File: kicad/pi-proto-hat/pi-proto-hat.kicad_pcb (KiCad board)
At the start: 2 copper layers, 65 x 56 mm, 5 parts, among them P1 Conn_02x20_Odd_Even

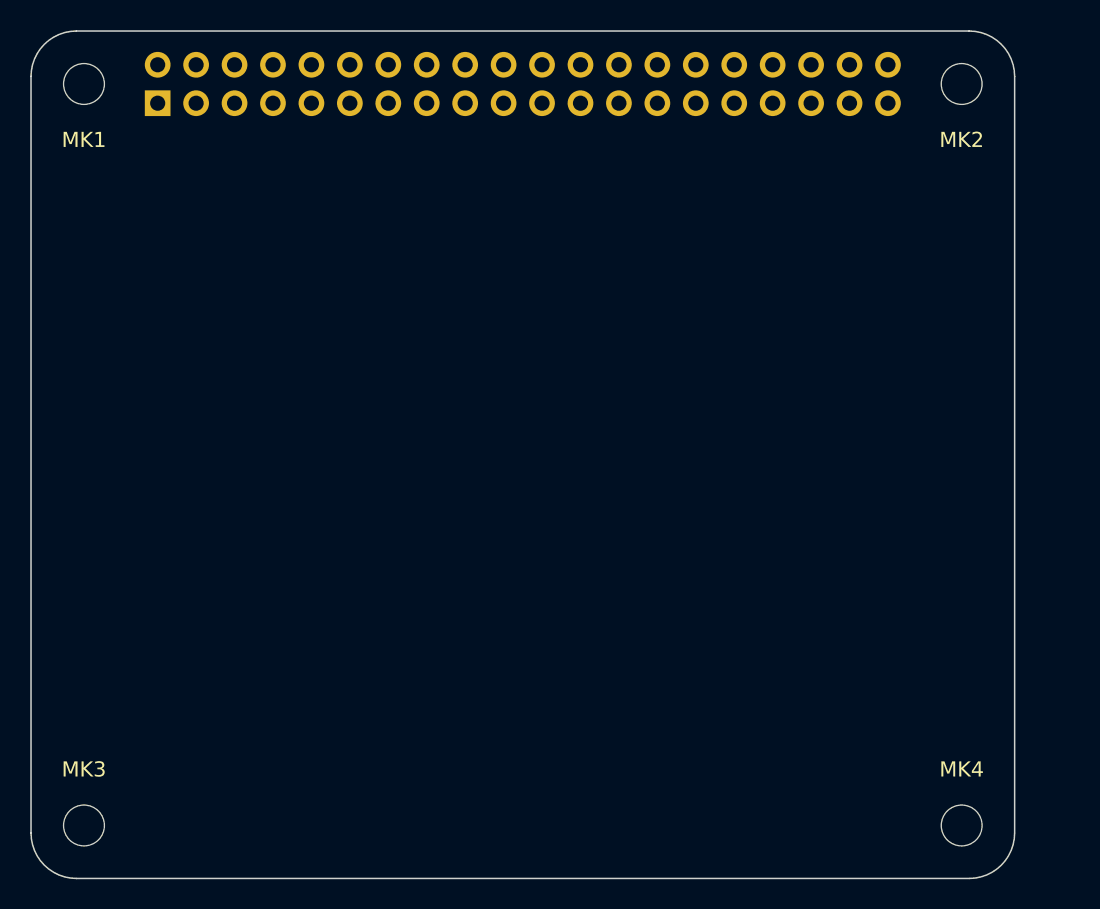
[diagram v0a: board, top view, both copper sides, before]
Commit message: R1: one GPIO connector, one I2C connector
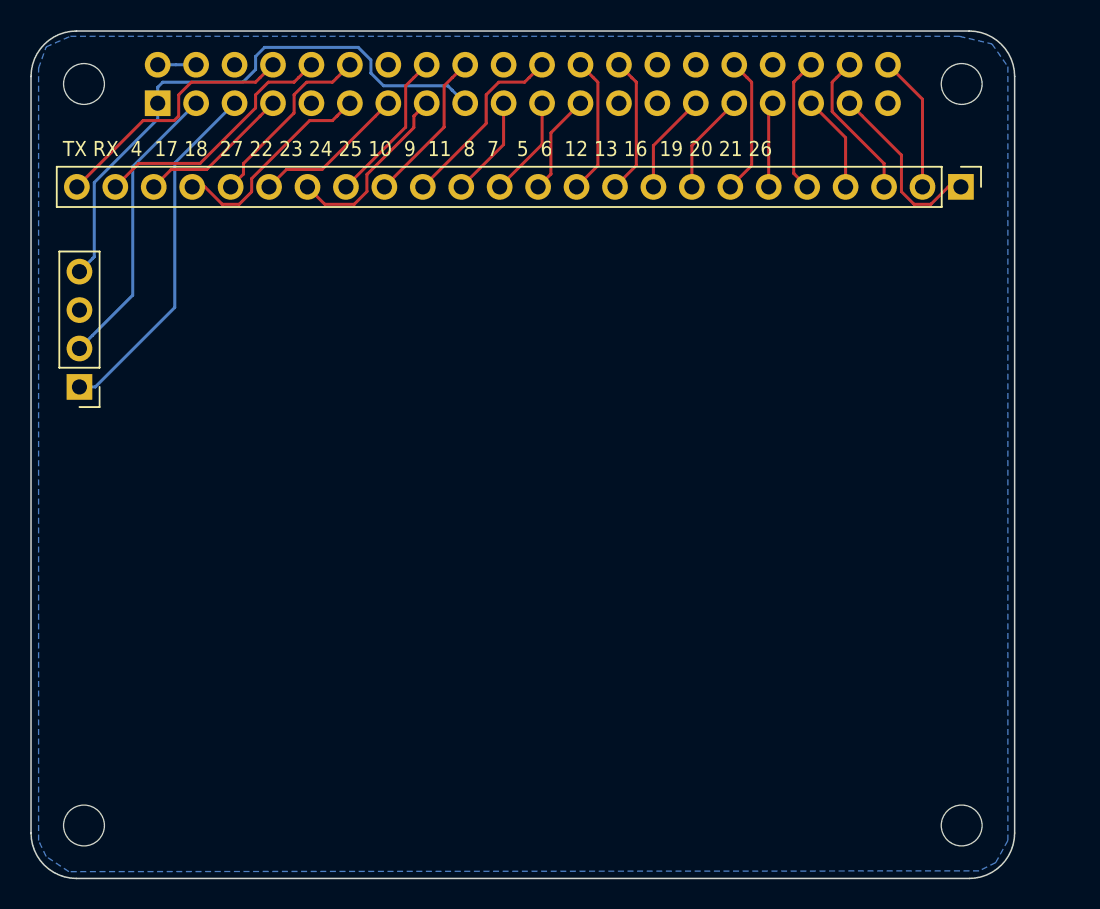
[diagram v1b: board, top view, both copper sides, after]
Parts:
- added J1: Conn_01x24_Male, Connector_PinHeader_2.54mm:PinHeader_1x24_P2.54mm_Vertical, F.Cu at (261.4, 104.3)
- added J2: Conn_I2C, Connector_PinHeader_2.54mm:PinHeader_1x04_P2.54mm_Vertical, F.Cu at (203.2, 117.5)
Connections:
- net /ID_SC renamed Net-(P1-Pad28)
- net /ID_SD renamed Net-(P1-Pad27)
- P1 pad 24: /GPIO8(SPI0_CE_N) -> /GPIO8(SPI0_CE_0)
- P1 pad 26: /GPIO7(SPI1_CE_N) -> /GPIO7(SPI1_CE_1)
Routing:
- net +3V3: track 0.00 -> 38.3 mm
- net /GPIO3(SCL1): track 0.00 -> 23.6 mm
- net /GPIO2(SDA1): track 0.00 -> 19.4 mm
- net /GPIO14(TXD0): track 0.00 -> 17.1 mm
- net /GPIO15(RXD0): track 0.00 -> 16.8 mm
- net /GPIO17(GEN0): track 0.00 -> 14.2 mm
- net /GPIO25(GEN6): track 0.00 -> 12.3 mm
- net /GPIO18(GEN1)(PWM0): track 0.00 -> 12.3 mm
- net /GPIO22(GEN3): track 0.00 -> 12.2 mm
- net /GPIO26: track 0.00 -> 12.0 mm
- net /GPIO24(GEN5): track 0.00 -> 10.3 mm
- net /GPIO23(GEN4): track 0.00 -> 10.3 mm
- net /GPIO27(GEN2): track 0.00 -> 10.2 mm
- net /GPIO4(GCLK): track 0.00 -> 10.2 mm
- net /GPIO20(SPI1_MOSI): track 0.00 -> 9.97 mm
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- added copper zone on B.Cu, net GND
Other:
- board text added: "TX RX 4 17 18 27 22 23 24 25 10 9 11 8 7 5 6 12 13 16 19 20 21 26"

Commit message: R2: 1xUART+GND, 2xI2C+VCC+GND
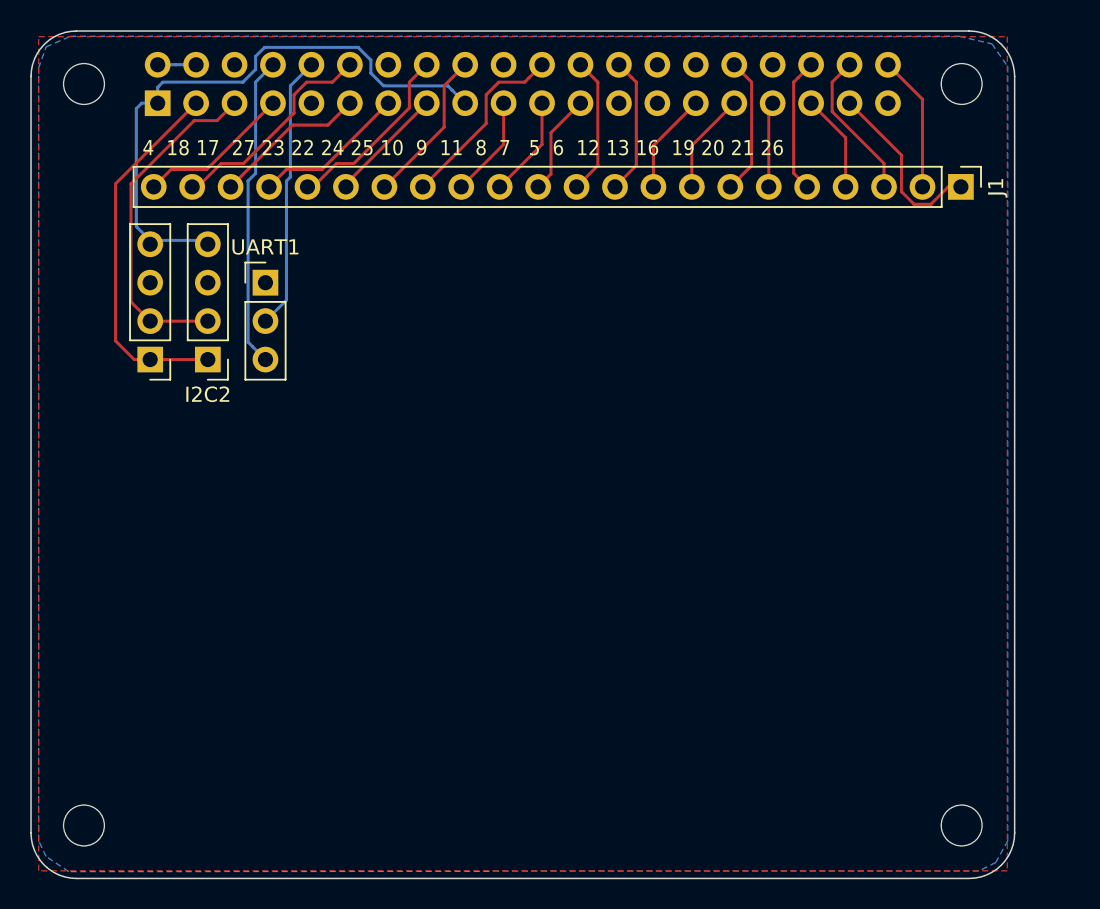
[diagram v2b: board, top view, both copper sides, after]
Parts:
- added I2C2: Conn_I2C, Connector_PinHeader_2.54mm:PinHeader_1x04_P2.54mm_Vertical, F.Cu at (211.7, 115.7)
- added UART1: Conn_01x03_Male, Connector_PinHeader_2.54mm:PinHeader_1x03_P2.54mm_Vertical, F.Cu at (215.5, 110.6)
- J1: value Conn_01x24_Male -> Conn_01x22_Male; footprint Connector_PinHeader_2.54mm:PinHeader_1x24_P2.54mm_Vertical -> Connector_PinHeader_2.54mm:PinHeader_1x22_P2.54mm_Vertical
- moved I2C1 5.01 mm to (207.9, 115.7)
- renumbered J2 to I2C1
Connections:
- I2C1 pad 1: /GPIO3(SCL1) -> /GPIO2(SDA1)
- I2C1 pad 2: /GPIO2(SDA1) -> /GPIO3(SCL1)
- J1 pad 17: /GPIO23(GEN4) -> /GPIO22(GEN3)
- J1 pad 18: /GPIO22(GEN3) -> /GPIO23(GEN4)
- J1 pad 20: /GPIO18(GEN1)(PWM0) -> /GPIO17(GEN0)
- J1 pad 21: /GPIO17(GEN0) -> /GPIO18(GEN1)(PWM0)
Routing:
- net /GPIO2(SDA1): track 19.4 -> 24.5 mm
- net /GPIO22(GEN3): track 12.2 -> 7.74 mm
- net /GPIO17(GEN0): track 14.2 -> 10.2 mm
- net /GPIO14(TXD0): track 17.1 -> 20.6 mm
- net /GPIO18(GEN1)(PWM0): track 12.3 -> 14.5 mm
- net /GPIO23(GEN4): track 10.3 -> 12.2 mm
- net /GPIO15(RXD0): track 16.8 -> 18.2 mm
- net /GPIO3(SCL1): track 23.6 -> 22.5 mm
- added copper zone on F.Cu, net GND
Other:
- net class Power: trace_width 0.5 -> 1.2
- board text added: "4 18 17 27 23 22 24 25 10 9 11 8 7 5 6 12 13 16 19 20 21 26"
- board text removed: "TX RX 4 17 18 27 22 23 24 25 10 9 11 8 7 5 6 12 13 16 19 20 21 26"

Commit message: R3: VCC+GND connector 22x02
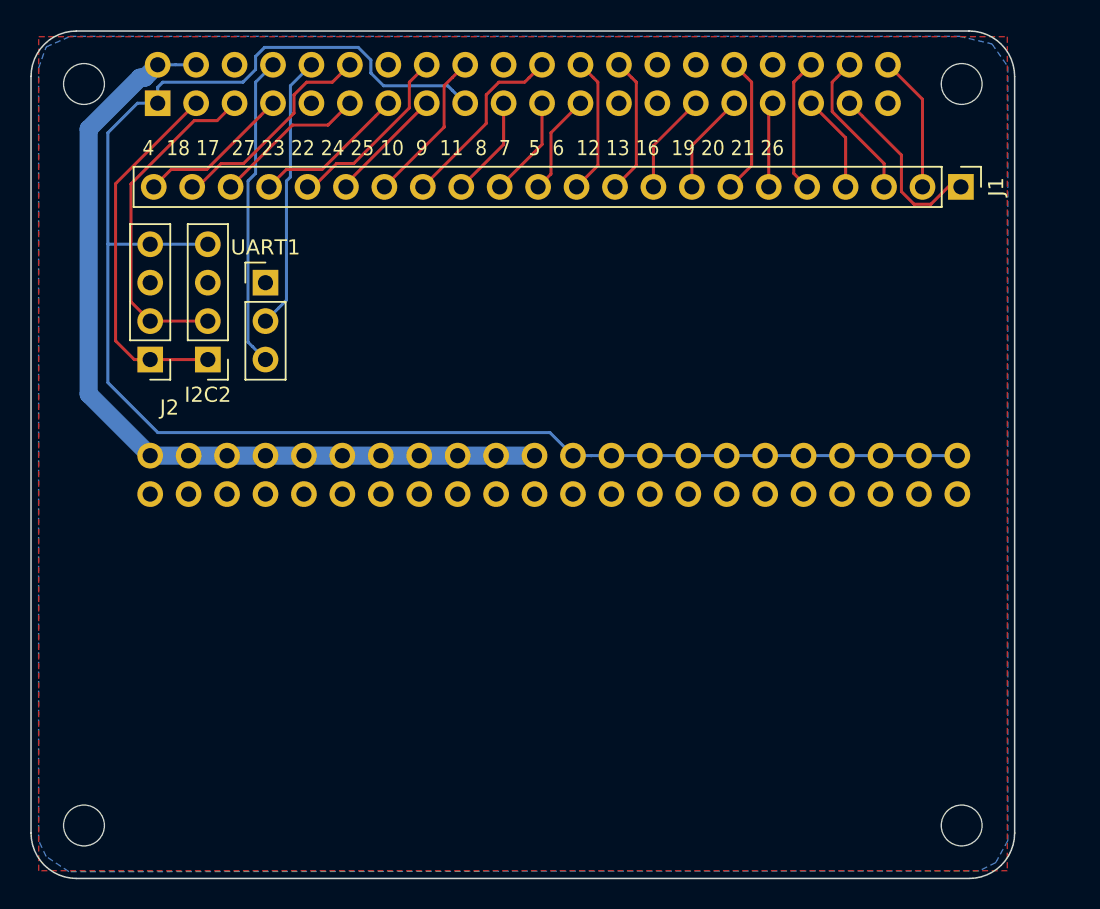
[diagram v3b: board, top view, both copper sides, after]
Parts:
- added J2: Conn_02x22_Top_Bottom, Proto_Area:Proto_Area_22x02, F.Cu at (207.9, 122.1)
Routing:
- net +3V3: track 38.7 -> 110.4 mm
- net +5V: track 2.54 -> 57.5 mm
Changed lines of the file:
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@@
     (thickness 1.6)
     (drawings 25)
-    (tracks 126)
+    (tracks 137)
     (zones 0)
-    (modules 9)
+    (modules 10)
     (nets 32)
   )
@@
     (add_net +5V)
   )
+  (module Proto_Area:Proto_Area_22x02 (layer F.Cu)
+    (at 207.874 122.06)
+    (descr "Prototyping Area")
+    (tags connector)
+    (attr virtual)
+    (fp_text reference J2 (at 1.27 -3.175) (layer F.SilkS)
+      (effects (font (size 1 1) (thickness 0.15)))
+    )
+    (fp_text value Conn_02x22_Top_Bottom (at 1.27 5.08) (layer F.Fab)
+      (effects (font (size 1 1) (thickness 0.15)))
+    )
+    (fp_line (start 54.61 -1.27) (end 54.61 3.81) (layer F.CrtYd) (width 0.05))
+    (fp_line (start -1.27 3.81) (end 54.61 3.81) (layer F.CrtYd) (width 0.05))
+    (fp_line (start -1.27 -1.27) (end -1.27 3.81) (layer F.CrtYd) (width 0.05))
+    (fp_line (start -1.27 -1.27) (end 54.61 -1.27) (layer F.CrtYd) (width 0.05))
+    (fp_text user %R (at 1.27 1.27) (layer F.Fab)
+      (effects (font (size 1 1) (thickness 0.15)))
+    )
+    (pad 44 thru_hole circle (at 53.34 2.54) (size 1.7 1.7) (drill 1) (layers *.Cu *.Mask)
+      (net 3 GND))
+    (pad 22 thru_hole circle (at 53.34 0) (size 1.7 1.7) (drill 1) (layers *.Cu *.Mask)
+      (net 1 +3V3))
+    (pad 43 thru_hole circle (at 50.8 2.54) (size 1.7 1.7) (drill 1) (layers *.Cu *.Mask)
+      (net 3 GND))
+    (pad 21 thru_hole circle (at 50.8 0) (size 1.7 1.7) (drill 1) (layers *.Cu *.Mask)
+      (net 1 +3V3))
+    (pad 42 thru_hole circle (at 48.26 2.54) (size 1.7 1.7) (drill 1) (layers *.Cu *.Mask)
+      (net 3 GND))
+    (pad 20 thru_hole circle (at 48.26 0) (size 1.7 1.7) (drill 1) (layers *.Cu *.Mask)
+      (net 1 +3V3))
+    (pad 41 thru_hole circle (at 45.72 2.54) (size 1.7 1.7) (drill 1) (layers *.Cu *.Mask)
+      (net 3 GND))
+    (pad 19 thru_hole circle (at 45.72 0) (size 1.7 1.7) (drill 1) (layers *.Cu *.Mask)
+      (net 1 +3V3))
+    (pad 40 thru_hole circle (at 43.18 2.54) (size 1.7 1.7) (drill 1) (layers *.Cu *.Mask)
+      (net 3 GND))
+    (pad 18 thru_hole circle (at 43.18 0) (size 1.7 1.7) (drill 1) (layers *.Cu *.Mask)
+      (net 1 +3V3))
+    (pad 39 thru_hole circle (at 40.64 2.54) (size 1.7 1.7) (drill 1) (layers *.Cu *.Mask)
+      (net 3 GND))
+    (pad 17 thru_hole circle (at 40.64 0) (size 1.7 1.7) (drill 1) (layers *.Cu *.Mask)
+      (net 1 +3V3))
+    (pad 38 thru_hole circle (at 38.1 2.54) (size 1.7 1.7) (drill 1) (layers *.Cu *.Mask)
+      (net 3 GND))
+    (pad 16 thru_hole circle (at 38.1 0) (size 1.7 1.7) (drill 1) (layers *.Cu *.Mask)
+      (net 1 +3V3))
+    (pad 37 thru_hole circle (at 35.56 2.54) (size 1.7 1.7) (drill 1) (layers *.Cu *.Mask)
+      (net 3 GND))
+    (pad 15 thru_hole circle (at 35.56 0) (size 1.7 1.7) (drill 1) (layers *.Cu *.Mask)
+      (net 1 +3V3))
+    (pad 36 thru_hole circle (at 33.02 2.54) (size 1.7 1.7) (drill 1) (layers *.Cu *.Mask)
+      (net 3 GND))
+    (pad 14 thru_hole circle (at 33.02 0) (size 1.7 1.7) (drill 1) (layers *.Cu *.Mask)
+      (net 1 +3V3))
+    (pad 35 thru_hole circle (at 30.48 2.54) (size 1.7 1.7) (drill 1) (layers *.Cu *.Mask)
+      (net 3 GND))
+    (pad 13 thru_hole circle (at 30.48 0) (size 1.7 1.7) (drill 1) (layers *.Cu *.Mask)
+      (net 1 +3V3))
+    (pad 34 thru_hole circle (at 27.94 2.54) (size 1.7 1.7) (drill 1) (layers *.Cu *.Mask)
+      (net 3 GND))
+    (pad 12 thru_hole circle (at 27.94 0) (size 1.7 1.7) (drill 1) (layers *.Cu *.Mask)
+      (net 1 +3V3))
+    (pad 33 thru_hole circle (at 25.4 2.54) (size 1.7 1.7) (drill 1) (layers *.Cu *.Mask)
+      (net 3 GND))
+    (pad 11 thru_hole circle (at 25.4 0) (size 1.7 1.7) (drill 1) (layers *.Cu *.Mask)
+      (net 2 +5V))
+    (pad 32 thru_hole circle (at 22.86 2.54) (size 1.7 1.7) (drill 1) (layers *.Cu *.Mask)
+      (net 3 GND))
+    (pad 10 thru_hole circle (at 22.86 0) (size 1.7 1.7) (drill 1) (layers *.Cu *.Mask)
+      (net 2 +5V))
+    (pad 31 thru_hole circle (at 20.32 2.54) (size 1.7 1.7) (drill 1) (layers *.Cu *.Mask)
+      (net 3 GND))
+    (pad 9 thru_hole circle (at 20.32 0) (size 1.7 1.7) (drill 1) (layers *.Cu *.Mask)
+      (net 2 +5V))
+    (pad 30 thru_hole circle (at 17.78 2.54) (size 1.7 1.7) (drill 1) (layers *.Cu *.Mask)
+      (net 3 GND))
+    (pad 8 thru_hole circle (at 17.78 0) (size 1.7 1.7) (drill 1) (layers *.Cu *.Mask)
+      (net 2 +5V))
+    (pad 29 thru_hole circle (at 15.24 2.54) (size 1.7 1.7) (drill 1) (layers *.Cu *.Mask)
+      (net 3 GND))
+    (pad 7 thru_hole circle (at 15.24 0) (size 1.7 1.7) (drill 1) (layers *.Cu *.Mask)
+      (net 2 +5V))
+    (pad 28 thru_hole circle (at 12.7 2.54) (size 1.7 1.7) (drill 1) (layers *.Cu *.Mask)
+      (net 3 GND))
+    (pad 6 thru_hole circle (at 12.7 0) (size 1.7 1.7) (drill 1) (layers *.Cu *.Mask)
+      (net 2 +5V))
+    (pad 27 thru_hole circle (at 10.16 2.54) (size 1.7 1.7) (drill 1) (layers *.Cu *.Mask)
+      (net 3 GND))
+    (pad 5 thru_hole circle (at 10.16 0) (size 1.7 1.7) (drill 1) (layers *.Cu *.Mask)
+      (net 2 +5V))
+    (pad 26 thru_hole circle (at 7.62 2.54) (size 1.7 1.7) (drill 1) (layers *.Cu *.Mask)
+      (net 3 GND))
+    (pad 4 thru_hole circle (at 7.62 0) (size 1.7 1.7) (drill 1) (layers *.Cu *.Mask)
+      (net 2 +5V))
+    (pad 25 thru_hole circle (at 5.08 2.54) (size 1.7 1.7) (drill 1) (layers *.Cu *.Mask)
+      (net 3 GND))
+    (pad 3 thru_hole circle (at 5.08 0) (size 1.7 1.7) (drill 1) (layers *.Cu *.Mask)
+      (net 2 +5V))
+    (pad 24 thru_hole circle (at 2.54 2.54) (size 1.7 1.7) (drill 1) (layers *.Cu *.Mask)
+      (net 3 GND))
+    (pad 2 thru_hole circle (at 2.54 0) (size 1.7 1.7) (drill 1) (layers *.Cu *.Mask)
+      (net 2 +5V))
+    (pad 23 thru_hole circle (at 0 2.54) (size 1.7 1.7) (drill 1) (layers *.Cu *.Mask)
+      (net 3 GND))
+    (pad 1 thru_hole circle (at 0 0) (size 1.7 1.7) (drill 1) (layers *.Cu *.Mask)
+      (net 2 +5V))
+  )
   (module Connector_PinSocket_2.54mm:PinSocket_2x20_P2.54mm_Vertical (layer B.Cu)
     (at 208.37 98.77 270)
@@
   (segment (start 208.37 97.72) (end 208.709999 97.380001) (width 0.2) (layer B.Cu) (net 1))
   (segment (start 208.37 98.77) (end 208.37 97.72) (width 0.2) (layer B.Cu) (net 1))
-  (segment (start 206.959999 106.921999) (end 207.024001 106.986001) (width 0.2) (layer B.Cu) (net 1))
-  (segment (start 207.024001 106.986001) (end 207.874 107.836) (width 0.2) (layer B.Cu) (net 1))
-  (segment (start 206.959999 99.130001) (end 206.959999 106.921999) (width 0.2) (layer B.Cu) (net 1))
-  (segment (start 207.32 98.77) (end 206.959999 99.130001) (width 0.2) (layer B.Cu) (net 1))
-  (segment (start 208.37 98.77) (end 207.32 98.77) (width 0.2) (layer B.Cu) (net 1))
-  (segment (start 207.874 107.836) (end 210.922 107.836) (width 0.2) (layer B.Cu) (net 1))
+  (segment (start 237.016081 122.06) (end 261.214 122.06) (width 0.2) (layer B.Cu) (net 1))
+  (segment (start 235.814 122.06) (end 237.016081 122.06) (width 0.2) (layer B.Cu) (net 1))
+  (segment (start 234.29 120.536) (end 235.814 122.06) (width 0.2) (layer B.Cu) (net 1))
+  (segment (start 205.08 117.234) (end 208.382 120.536) (width 0.2) (layer B.Cu) (net 1))
+  (segment (start 208.37 98.77) (end 207.034 98.77) (width 0.2) (layer B.Cu) (net 1))
+  (segment (start 208.382 120.536) (end 234.29 120.536) (width 0.2) (layer B.Cu) (net 1))
+  (segment (start 207.034 98.77) (end 205.08 100.724) (width 0.2) (layer B.Cu) (net 1))
+  (segment (start 207.874 108.09) (end 205.08 108.09) (width 0.2) (layer B.Cu) (net 1))
+  (segment (start 205.08 100.724) (end 205.08 108.09) (width 0.2) (layer B.Cu) (net 1))
+  (segment (start 205.08 108.09) (end 205.08 117.234) (width 0.2) (layer B.Cu) (net 1))
+  (segment (start 207.874 108.09) (end 211.684 108.09) (width 0.2) (layer B.Cu) (net 1))
   (segment (start 209.572081 96.23) (end 210.91 96.23) (width 0.2) (layer B.Cu) (net 2))
   (segment (start 208.37 96.23) (end 209.572081 96.23) (width 0.2) (layer B.Cu) (net 2))
+  (segment (start 203.81 100.47) (end 203.81 117.996) (width 1.2) (layer B.Cu) (net 2))
+  (segment (start 207.200001 97.079999) (end 203.81 100.47) (width 1.2) (layer B.Cu) (net 2))
+  (segment (start 203.81 117.996) (end 207.874 122.06) (width 1.2) (layer B.Cu) (net 2))
+  (segment (start 208.37 96.23) (end 207.520001 97.079999) (width 1.2) (layer B.Cu) (net 2))
+  (segment (start 207.520001 97.079999) (end 207.200001 97.079999) (width 1.2) (layer B.Cu) (net 2))
+  (segment (start 207.874 122.06) (end 233.274 122.06) (width 1.2) (layer B.Cu) (net 2))
   (segment (start 241.13 101.57) (end 243.93 98.77) (width 0.2) (layer F.Cu) (net 4))
   (segment (start 241.13 104.3) (end 241.13 101.57) (width 0.2) (layer F.Cu) (net 4))
